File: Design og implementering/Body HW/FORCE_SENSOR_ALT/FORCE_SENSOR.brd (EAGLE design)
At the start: 68.6 x 47.1 mm, 15 parts, among them IC1 MCP6004P, J1 RJ11-6PTH, J2 RJ11-6PTH

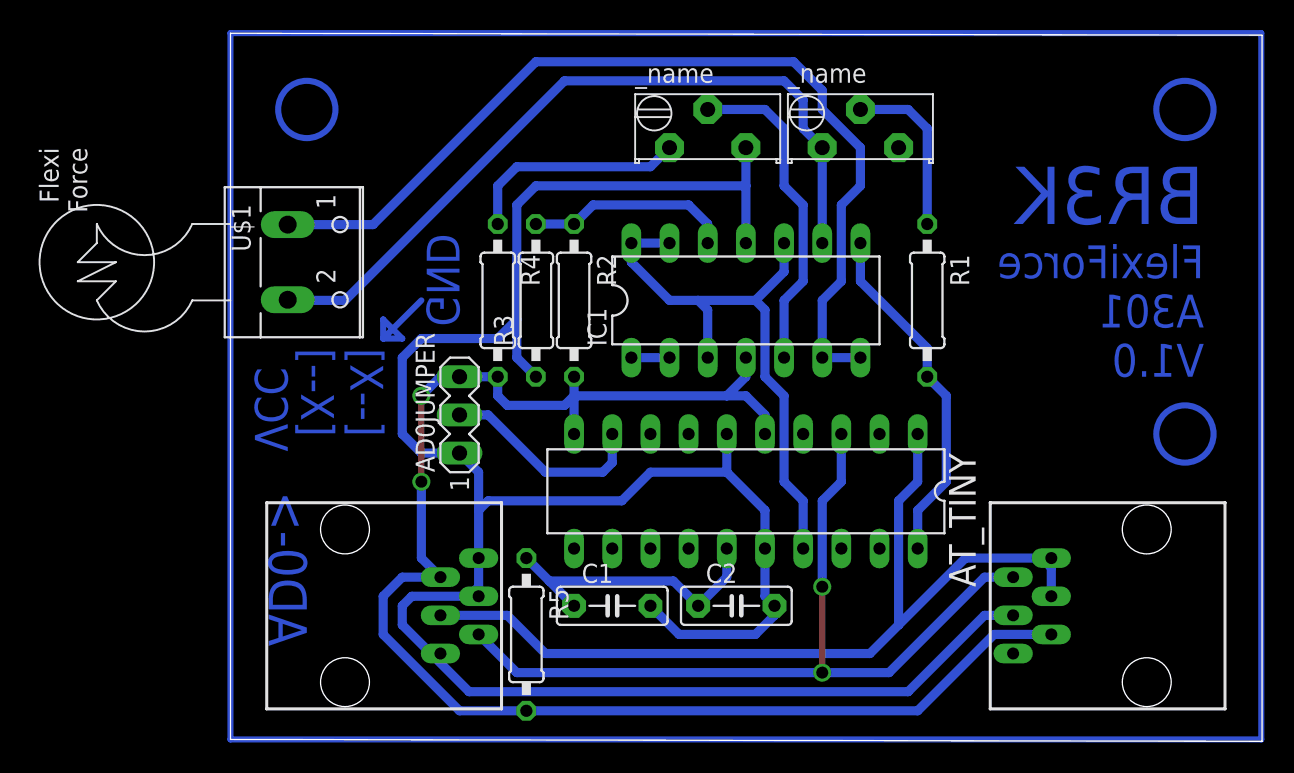
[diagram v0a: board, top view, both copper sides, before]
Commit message: Added improved Force sensor design -Felix
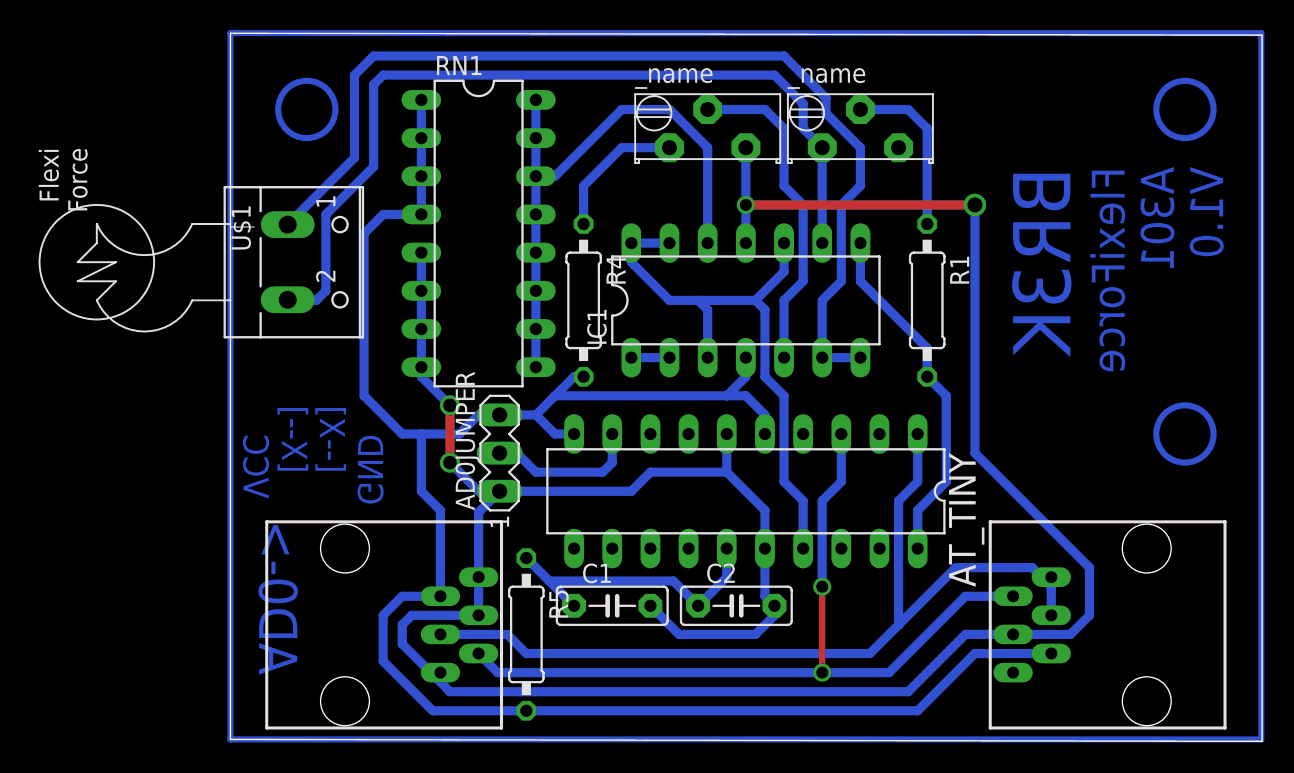
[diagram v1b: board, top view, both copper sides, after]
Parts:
- removed R2, R3: 1M Ohm, resistor:0207/10
- added RN1: 240kOhm, resistor-dil:DIL16
- moved R4 5.71 mm to (26.0, 53.3)
- moved AD0JUMPER 3.68 mm to (20.4, 43.2)
- moved J1 1.27 mm to (10.2, 36.8)
- moved J2 1.27 mm to (63.5, 26.7)
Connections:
- removed net N$2: IC1.12, R2.1, R3.2
- new net N$11: IC1.12, RN1.10, RN1.11, RN1.12, RN1.13, RN1.14, RN1.15, RN1.16, RN1.9
- net GND: now also RN1.5, RN1.6, RN1.7, RN1.8; no longer R3.1
- net VCC: now also RN1.1, RN1.2, RN1.3, RN1.4; no longer R2.2
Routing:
- net N$11: track 0.00 -> 38.5 mm
- net VCC: track 102.0 -> 128.4 mm, vias 2 -> 0
- net GND: track 154.2 -> 174.1 mm, vias 0 -> 4
- net N$2: track 13.8 -> 0.00 mm
- net N$8: track 7.93 -> 0.00 mm
- net N$5: track 51.0 -> 57.4 mm
- net N$1: track 15.0 -> 9.31 mm
- net AD0_SELECT: track 13.9 -> 10.2 mm
- net SENS_SUPPLY: track 63.3 -> 66.7 mm
- net SCL: track 55.6 -> 54.6 mm
- net SDA: track 59.7 -> 59.2 mm
